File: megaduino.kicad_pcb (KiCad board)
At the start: 2 copper layers, 48.9 x 52.7 mm, 36 parts, among them J1 Conn_01x20_Female, J2 Conn_01x20_Female, J3 Conn_01x13_Male, J4 Conn_01x02_Male, J5 Conn_01x04_Male, Q1 RFD14N05L, Q2 RFD14N05L, U1 LMV324, U2 MCP2562-E-SN, U3 LMV324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

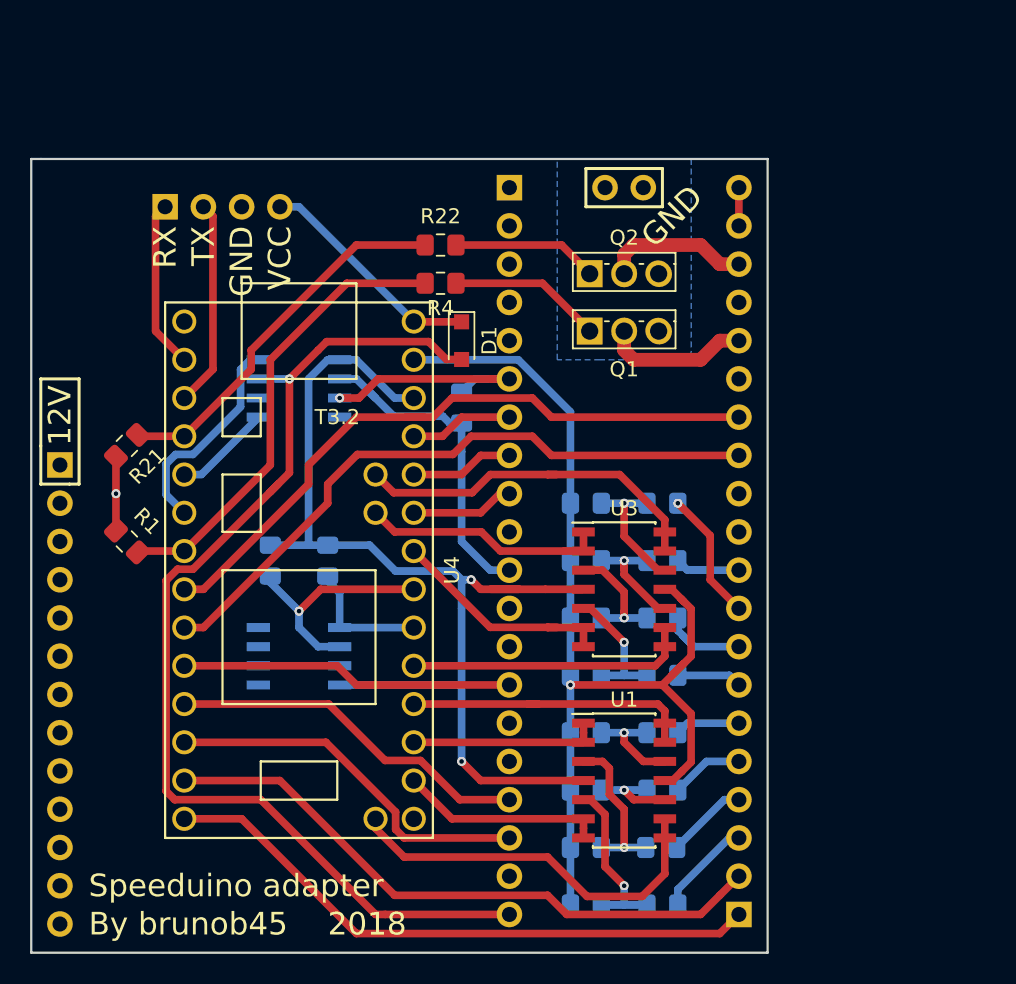
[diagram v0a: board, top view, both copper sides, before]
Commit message: the HC connector was 180 deg; begin corrections
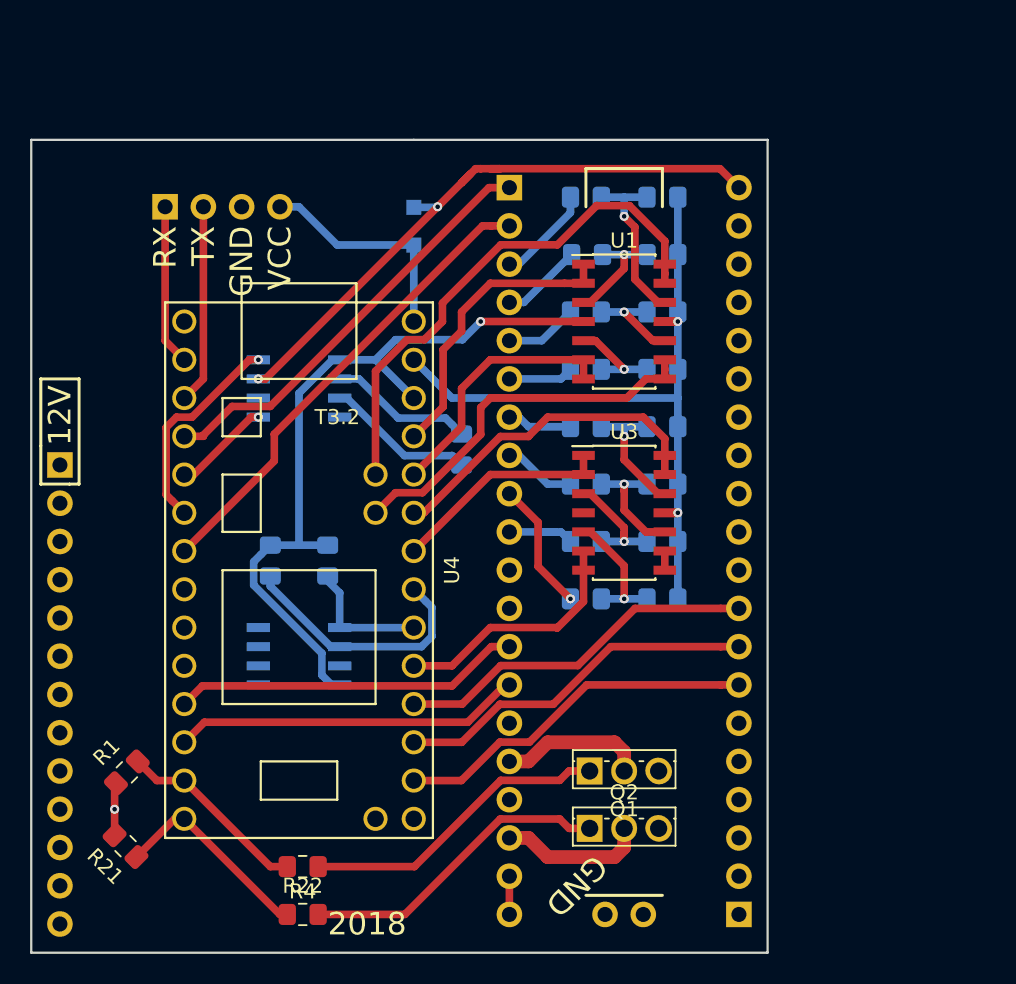
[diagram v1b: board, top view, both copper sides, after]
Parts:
- D1: moved to B.Cu
- moved J1 50.6 mm to (165.1, 116.8), turned to 0 degrees
- moved J2 50.6 mm to (149.9, 68.6), turned to 180 degrees
- moved J4 48.3 mm to (156.2, 116.8)
- moved R7 47.3 mm to (154.9, 69.2), turned to 0 degrees
- moved R8 47.3 mm to (160.0, 69.2), turned to 0 degrees
- moved R22 45.4 mm to (136.1, 116.8)
- moved R4 39.8 mm to (136.1, 113.7)
- moved R6 39.7 mm to (160.0, 73.0), turned to 0 degrees
- moved R5 39.7 mm to (155.0, 73.0), turned to 0 degrees
- moved Q2 36.8 mm to (155.2, 111.1)
- moved R10 32.2 mm to (160.0, 76.8), turned to 0 degrees
- moved R9 32.2 mm to (154.9, 76.8), turned to 0 degrees
- moved U1 30.5 mm to (157.5, 77.5)
- moved Q1 29.2 mm to (155.2, 107.3)
- moved R21 26.6 mm to (124.4, 112.3), turned to 315 degrees
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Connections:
- U1 pad 12: Net-(R11-Pad2) -> Net-(R7-Pad2)
- U1 pad 13: A3 -> A0
- U1 pad 14: A3 -> A0
- U1 pad 5: Net-(R7-Pad2) -> Net-(R11-Pad2)
- U1 pad 6: A0 -> A3
- U1 pad 7: A0 -> A3
- U4 pad 11: IRQ1 -> FP
- U4 pad 12: FAN -> Idle
- U4 pad 13: INJ2 -> INJ4
- U4 pad 14: INJ1 -> INJ3
- U4 pad 19: A2 -> A7
- U4 pad 21: A0 -> IGN1
- U4 pad 22: A1 -> IGN2
- U4 pad 23: A3 -> ECL
- U4 pad 24: A7 -> A4
- U4 pad 27: A4 -> A5
- U4 pad 28: ECL -> A6
- U4 pad 29: IGN2 -> A3
- U4 pad 30: IGN1 -> A1
- U4 pad 36: A6 -> A0
- U4 pad 37: A5 -> A2
- U4 pad 4: INJ3 -> INJ1
- U4 pad 7: INJ4 -> INJ2
- U4 pad 8: Idle -> FAN
- U4 pad 9: FP -> IRQ1
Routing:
- net +5V: track 73.3 -> 41.2 mm, vias 1 -> 2
- net FAN: track 24.9 -> 0.00 mm
- net IRQ1: track 24.2 -> 0.00 mm
- net IRQ0: track 22.1 -> 0.00 mm
- net GNDA: track 68.8 -> 47.0 mm, vias 1 -> 2
- net A0: track 13.6 -> 35.1 mm
- net Idle: track 44.5 -> 23.2 mm
- net +3V3: track 72.3 -> 51.2 mm, vias 2 -> 1
- net FP: track 43.4 -> 23.2 mm
- net A7: track 19.3 -> 1.27 mm
- net INJ4: track 30.2 -> 12.8 mm
- net IGN2: track 6.88 -> 24.2 mm
- net IGN1: track 6.88 -> 24.2 mm
- net ECL: track 6.88 -> 24.2 mm
- net CANL: track 22.0 -> 9.61 mm
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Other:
- board size 48.9 x 52.7 mm -> 48.9 x 54 mm
- board text removed: "By brunob45"
- board text removed: "Speeduino adapter"

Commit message: reverse HC connector pt2
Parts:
- moved R22 42.6 mm to (176.8, 104.1)
- moved R4 42.2 mm to (176.5, 101.6)
- moved U5 40.8 mm to (148.6, 61.0)
- moved R23 40.6 mm to (180.3, 63.3)
- moved R3 37.6 mm to (154.9, 59.9)
- moved R2 34.0 mm to (143.5, 60.7)
- moved U2 32.5 mm to (160.2, 60.3)
- moved R20 32.3 mm to (128.3, 90.2), turned to 180 degrees
- moved R8 32.3 mm to (128.3, 74.9), turned to 180 degrees
- moved R6 32.1 mm to (128.3, 77.5), turned to 180 degrees
- moved R10 31.9 mm to (128.3, 80.0), turned to 180 degrees
- moved R12 31.8 mm to (128.3, 82.5), turned to 180 degrees
- moved R14 31.8 mm to (128.3, 85.1), turned to 180 degrees
- moved R16 31.8 mm to (128.3, 87.6), turned to 180 degrees
- moved R18 31.8 mm to (128.3, 92.7), turned to 180 degrees
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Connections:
- J1 pad 1: (no net) -> Net-(J1-Pad1)
- J1 pad 10: (no net) -> JS7
- J1 pad 12: (no net) -> TX
- J1 pad 13: (no net) -> RX
- J1 pad 15: (no net) -> JS12
- J1 pad 16: (no net) -> +12V
- J1 pad 3: (no net) -> Net-(J1-Pad3)
- J1 pad 4: (no net) -> Net-(J1-Pad4)
- J1 pad 5: (no net) -> Net-(J1-Pad5)
- J2 pad 11: (no net) -> Net-(J2-Pad11)
- J2 pad 15: (no net) -> JS3
- J2 pad 17: (no net) -> JS1
- J3 pad 1: (no net) -> Net-(J3-Pad1)
- J3 pad 10: (no net) -> Net-(J3-Pad10)
- J3 pad 11: (no net) -> Net-(J3-Pad11)
- J3 pad 12: (no net) -> Net-(J3-Pad12)
- J3 pad 13: (no net) -> Net-(J3-Pad13)
- J3 pad 2: (no net) -> Net-(J3-Pad2)
- J3 pad 3: (no net) -> Net-(J3-Pad3)
- J3 pad 4: (no net) -> Net-(J3-Pad4)
- J3 pad 5: (no net) -> Net-(J3-Pad5)
- J3 pad 6: (no net) -> Net-(J3-Pad6)
- J3 pad 7: (no net) -> Net-(J3-Pad7)
- J3 pad 8: (no net) -> Net-(J3-Pad8)
- J3 pad 9: (no net) -> Net-(J3-Pad9)
- U4 pad 11: FP -> INJ2
- U4 pad 12: Idle -> INJ1
- U4 pad 13: INJ4 -> IRQ1
- U4 pad 14: INJ3 -> FAN
- U4 pad 19: A7 -> A2
- U4 pad 20: (no net) -> Net-(U4-Pad20)
- U4 pad 21: IGN1 -> A3
- U4 pad 22: IGN2 -> A1
- U4 pad 23: ECL -> A0
- U4 pad 28: A6 -> INJ4
- U4 pad 29: A3 -> INJ3
- U4 pad 30: A1 -> FP
- U4 pad 36: A0 -> A7
- U4 pad 37: A2 -> A6
- U4 pad 4: INJ1 -> Idle
- U4 pad 7: INJ2 -> IGN1
- U4 pad 8: FAN -> IGN2
- U4 pad 9: IRQ1 -> ECL
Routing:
- net +5V: track 41.2 -> 0.00 mm, vias 2 -> 0
- net GNDA: track 47.0 -> 19.5 mm
- net A0: track 35.1 -> 14.2 mm
- net Net-(Q2-Pad1): track 20.9 -> 0.00 mm
- net Net-(Q1-Pad1): track 20.7 -> 0.00 mm
- net INJ2: track 31.6 -> 12.3 mm
- net Idle: track 23.2 -> 6.13 mm
- net Net-(R2-Pad2): track 17.0 -> 0.00 mm
- net INJ1: track 28.5 -> 12.3 mm
- net Net-(D1-Pad1): track 15.0 -> 0.00 mm
- net Net-(U2-Pad4): track 14.1 -> 0.00 mm, vias 1 -> 0
- net INJ3: track 13.7 -> 0.00 mm
- net Net-(J5-Pad2): track 13.2 -> 0.00 mm
- net FP: track 23.2 -> 10.2 mm
- net INJ4: track 12.8 -> 0.00 mm
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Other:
- board text removed: "2018"

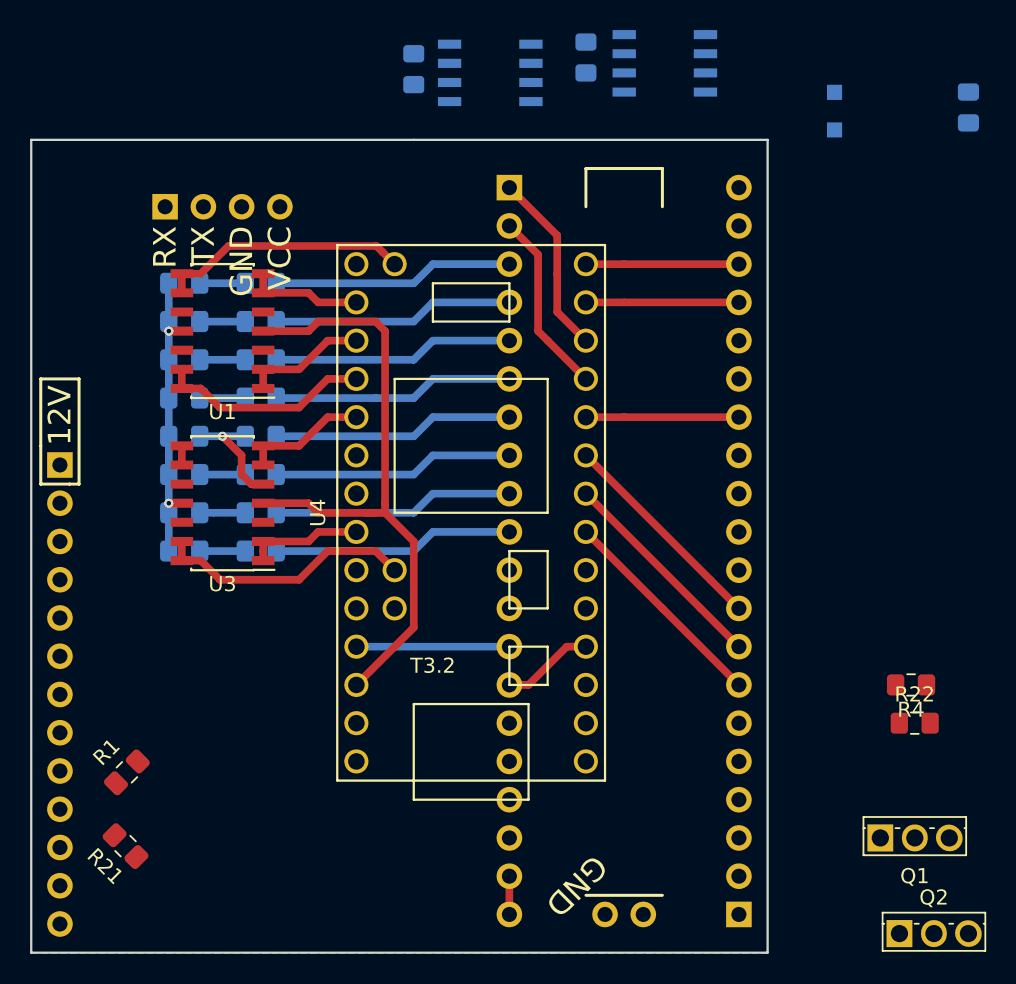
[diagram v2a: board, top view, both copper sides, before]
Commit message: reverse HC connector pt3
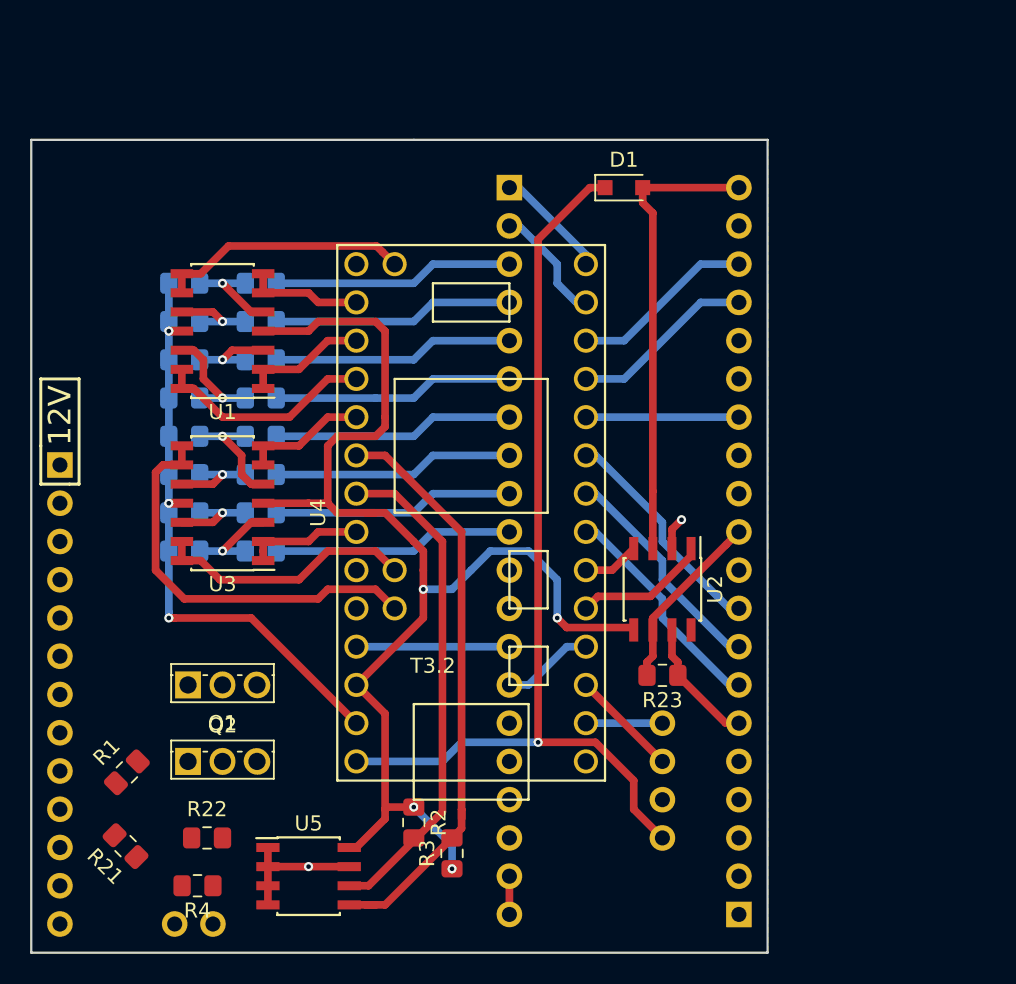
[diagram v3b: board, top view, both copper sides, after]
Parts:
- D1, R2, R23, R3, U2, U5: moved to F.Cu
- moved U5 54.7 mm to (136.5, 114.3)
- moved R3 53.6 mm to (146.1, 112.8), turned to 90 degrees
- moved R2 50.0 mm to (143.5, 110.7)
- moved R4 49.2 mm to (129.2, 114.9)
- moved Q2 48.6 mm to (128.5, 106.7)
- moved J5 47.6 mm to (160.0, 104.1), turned to 180 degrees
- moved R22 47.6 mm to (129.8, 111.8)
- moved Q1 47.1 mm to (128.5, 101.6)
- moved R23 42.8 mm to (160.0, 101.0), turned to 180 degrees
- moved U2 34.9 mm to (160.0, 95.2), turned to 270 degrees
- moved J4 28.6 mm to (127.6, 117.5)
- moved D1 14.9 mm to (157.5, 68.6), turned to 0 degrees
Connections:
- J1 pad 1: Net-(J1-Pad1) -> (no net)
- J1 pad 10: JS7 -> (no net)
- J1 pad 12: TX -> (no net)
- J1 pad 13: RX -> (no net)
- J1 pad 15: JS12 -> (no net)
- J1 pad 16: +12V -> (no net)
- J1 pad 3: Net-(J1-Pad3) -> (no net)
- J1 pad 4: Net-(J1-Pad4) -> (no net)
- J1 pad 5: Net-(J1-Pad5) -> (no net)
- J2 pad 11: Net-(J2-Pad11) -> (no net)
- J2 pad 15: JS3 -> (no net)
- J2 pad 17: JS1 -> (no net)
- J3 pad 1: Net-(J3-Pad1) -> (no net)
- J3 pad 10: Net-(J3-Pad10) -> (no net)
- J3 pad 11: Net-(J3-Pad11) -> (no net)
- J3 pad 12: Net-(J3-Pad12) -> (no net)
- J3 pad 13: Net-(J3-Pad13) -> (no net)
- J3 pad 2: Net-(J3-Pad2) -> (no net)
- J3 pad 3: Net-(J3-Pad3) -> (no net)
- J3 pad 4: Net-(J3-Pad4) -> (no net)
- J3 pad 5: Net-(J3-Pad5) -> (no net)
- J3 pad 6: Net-(J3-Pad6) -> (no net)
- J3 pad 7: Net-(J3-Pad7) -> (no net)
- J3 pad 8: Net-(J3-Pad8) -> (no net)
- J3 pad 9: Net-(J3-Pad9) -> (no net)
- U1 pad 10: Net-(R10-Pad1) -> Net-(R5-Pad2)
- U1 pad 12: Net-(R7-Pad2) -> Net-(R11-Pad2)
- U1 pad 13: A0 -> A3
- U1 pad 14: A0 -> A3
- U1 pad 3: Net-(R5-Pad2) -> Net-(R10-Pad1)
- U1 pad 5: Net-(R11-Pad2) -> Net-(R7-Pad2)
- U1 pad 6: A3 -> A0
- U1 pad 7: A3 -> A0
- U3 pad 1: A5 -> A7
- U3 pad 10: Net-(R17-Pad2) -> Net-(R15-Pad2)
- U3 pad 2: A5 -> A7
- U3 pad 3: Net-(R15-Pad2) -> Net-(R17-Pad2)
- U3 pad 8: A7 -> A5
- U3 pad 9: A7 -> A5
- U4 pad 11: INJ2 -> IRQ1
- U4 pad 12: INJ1 -> FAN
- U4 pad 13: IRQ1 -> INJ2
- U4 pad 14: FAN -> INJ1
- U4 pad 20: Net-(U4-Pad20) -> (no net)
- U4 pad 21: A3 -> A0
- U4 pad 23: A0 -> A3
- U4 pad 27: A5 -> A7
- U4 pad 36: A7 -> A5
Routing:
- net Net-(D1-Pad1): track 0.00 -> 63.9 mm, vias 0 -> 1
- net +3V3: track 43.5 -> 85.1 mm, vias 0 -> 4
- net Net-(R3-Pad2): track 0.00 -> 39.6 mm
- net Net-(R2-Pad2): track 0.00 -> 33.2 mm
- net +5V: track 0.00 -> 30.6 mm
- net GNDA: track 19.5 -> 39.3 mm, vias 2 -> 3
- net A5: track 7.72 -> 27.2 mm
- net CANL: track 0.00 -> 12.1 mm
- net Earth: track 0.00 -> 11.4 mm, vias 0 -> 2
- net Net-(U2-Pad1): track 0.00 -> 8.91 mm
- net CANH: track 0.00 -> 8.55 mm
- net Net-(J5-Pad2): track 0.00 -> 7.18 mm
- net A3: track 7.72 -> 14.7 mm
- net A7: track 1.27 -> 7.72 mm
- net A0: track 14.2 -> 7.72 mm
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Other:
- board text removed: "GND"
- board text removed: "RX"
- board text removed: "TX"
- board text removed: "VCC"

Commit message: reverse HC connector done
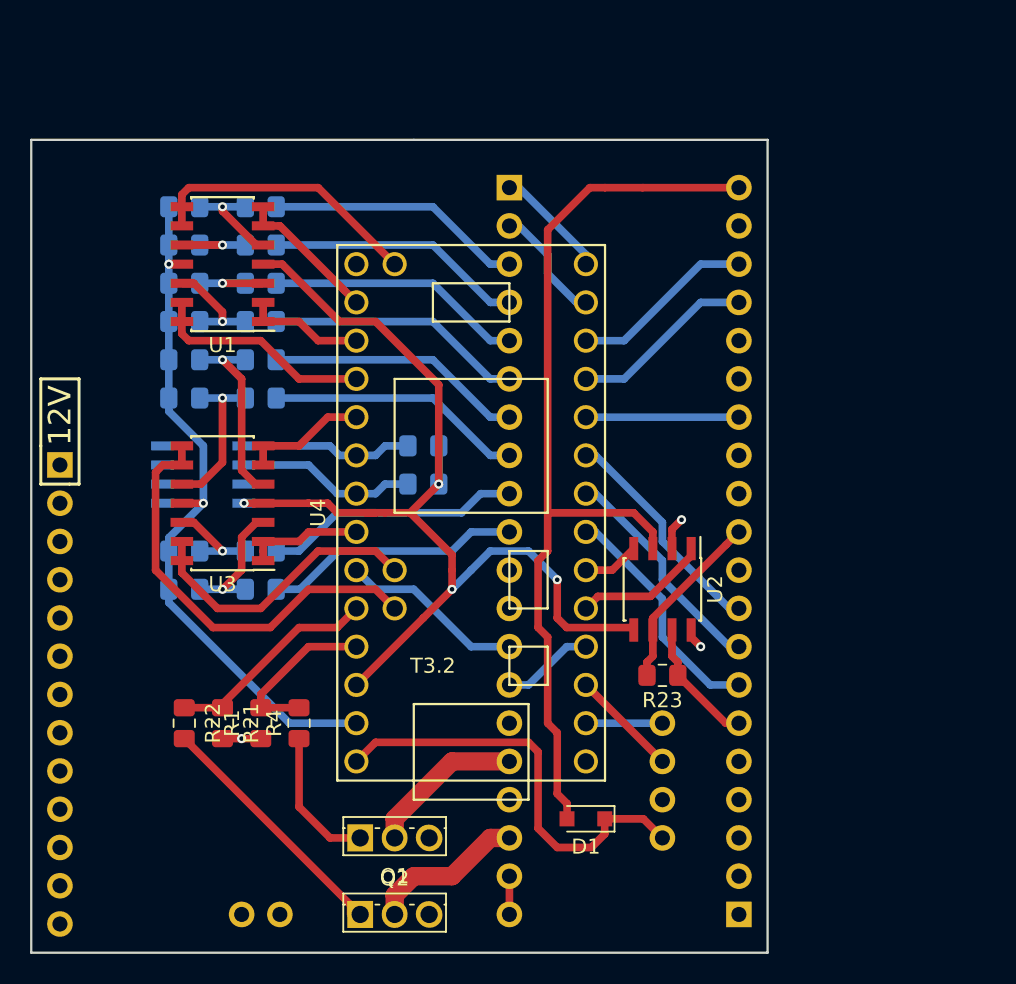
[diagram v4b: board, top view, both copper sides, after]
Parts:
- R2, R3, U5: moved to B.Cu
- moved D1 42.0 mm to (154.9, 110.5), turned to 180 degrees
- moved U5 27.6 mm to (129.5, 87.6)
- moved R3 27.1 mm to (144.1, 85.7), turned to 180 degrees
- moved R2 22.5 mm to (144.1, 88.3), turned to 180 degrees
- moved Q1 15.3 mm to (139.9, 111.8)
- moved Q2 15.3 mm to (139.9, 116.8)
- moved R4 12.7 mm to (135.9, 104.1), turned to 90 degrees
- moved R21 10.4 mm to (130.8, 104.1), turned to 90 degrees
- moved R1 9.47 mm to (133.3, 104.1), turned to 90 degrees
- moved R22 7.77 mm to (128.3, 104.1), turned to 90 degrees
- moved R7 5.08 mm to (133.3, 69.8)
- moved R8 5.08 mm to (128.3, 69.8)
- moved R10 5.08 mm to (128.3, 74.9)
- moved R11 5.08 mm to (133.3, 77.5)
- moved R12 5.08 mm to (128.3, 77.5)
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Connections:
- J1 pad 1: (no net) -> Net-(J1-Pad1)
- J1 pad 10: (no net) -> JS7
- J1 pad 12: (no net) -> TX
- J1 pad 13: (no net) -> RX
- J1 pad 15: (no net) -> JS12
- J1 pad 16: (no net) -> +12V
- J1 pad 3: (no net) -> Net-(J1-Pad3)
- J1 pad 4: (no net) -> Net-(J1-Pad4)
- J1 pad 5: (no net) -> Net-(J1-Pad5)
- J2 pad 11: (no net) -> Net-(J2-Pad11)
- J2 pad 15: (no net) -> JS3
- J2 pad 17: (no net) -> JS1
- J3 pad 1: (no net) -> Net-(J3-Pad1)
- J3 pad 10: (no net) -> Net-(J3-Pad10)
- J3 pad 11: (no net) -> Net-(J3-Pad11)
- J3 pad 12: (no net) -> Net-(J3-Pad12)
- J3 pad 13: (no net) -> Net-(J3-Pad13)
- J3 pad 2: (no net) -> Net-(J3-Pad2)
- J3 pad 3: (no net) -> Net-(J3-Pad3)
- J3 pad 4: (no net) -> Net-(J3-Pad4)
- J3 pad 5: (no net) -> Net-(J3-Pad5)
- J3 pad 6: (no net) -> Net-(J3-Pad6)
- J3 pad 7: (no net) -> Net-(J3-Pad7)
- J3 pad 8: (no net) -> Net-(J3-Pad8)
- J3 pad 9: (no net) -> Net-(J3-Pad9)
- U4 pad 20: (no net) -> D13
- U4 pad 28: INJ4 -> FP
- U4 pad 30: FP -> INJ4
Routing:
- net Net-(D1-Pad1): track 63.9 -> 28.6 mm, vias 1 -> 0
- net +5V: track 30.6 -> 62.7 mm
- net Net-(R3-Pad2): track 39.6 -> 11.4 mm
- net Net-(R2-Pad2): track 33.2 -> 11.9 mm
- net Net-(Q2-Pad1): track 0.00 -> 16.2 mm
- net +3V3: track 85.1 -> 70.7 mm
- net INJ3: track 0.00 -> 14.3 mm
- net INJ4: track 0.00 -> 11.1 mm
- net JS0: track 0.00 -> 10.5 mm
- net JS2: track 0.00 -> 10.5 mm
- net Net-(Q1-Pad1): track 0.00 -> 8.81 mm
- net GNDA: track 39.3 -> 46.2 mm, vias 3 -> 2
- net Earth: track 11.4 -> 6.09 mm, vias 2 -> 3
- net Net-(R13-Pad2): track 7.79 -> 12.7 mm
- net Net-(R15-Pad2): track 5.99 -> 10.6 mm
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
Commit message: minor changes
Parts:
- moved J5 2.54 mm to (160.0, 106.7)
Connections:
- U4 pad 2: Net-(J5-Pad1) -> Net-(J5-Pad2)
- U4 pad 3: Net-(J5-Pad2) -> Net-(J5-Pad1)
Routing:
- net +5V: track 62.7 -> 58.3 mm
- net Net-(J5-Pad1): track 5.08 -> 7.18 mm
- net Net-(D1-Pad1): track 28.6 -> 29.4 mm
- net INJ2: track 7.93 -> 7.18 mm
